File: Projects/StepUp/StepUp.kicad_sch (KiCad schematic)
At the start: 4 parts

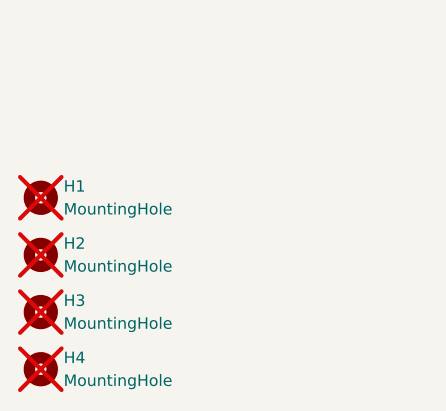
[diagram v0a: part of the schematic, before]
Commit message: feat(v0.2): Schematic updated, PCB layout start
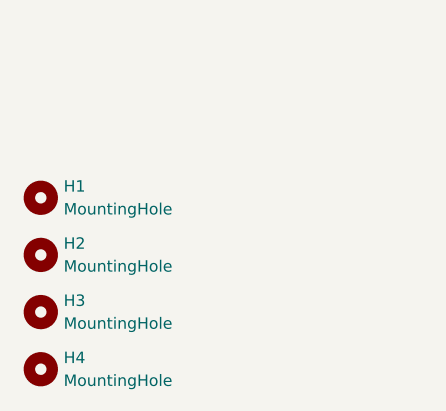
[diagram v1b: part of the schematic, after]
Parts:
- H1, H2, H3, H4: now fitted; now left out of the parts list
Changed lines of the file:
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@@
 		(title "System diagram")
 		(date "2024-04-28")
-		(rev "v0.1")
+		(rev "v0.2")
 		(company "SJFOM")
 	)
@@
 		(unit 1)
 		(exclude_from_sim no)
-		(in_bom yes)
-		(on_board yes)
-		(dnp yes)
+		(in_bom no)
+		(on_board yes)
+		(dnp no)
 		(fields_autoplaced yes)
 		(property "Reference" "H3"
@@
 		(unit 1)
 		(exclude_from_sim no)
-		(in_bom yes)
-		(on_board yes)
-		(dnp yes)
+		(in_bom no)
+		(on_board yes)
+		(dnp no)
 		(fields_autoplaced yes)
 		(property "Reference" "H4"
@@
 		(unit 1)
 		(exclude_from_sim no)
-		(in_bom yes)
-		(on_board yes)
-		(dnp yes)
+		(in_bom no)
+		(on_board yes)
+		(dnp no)
 		(fields_autoplaced yes)
 		(property "Reference" "H1"
@@
 		(unit 1)
 		(exclude_from_sim no)
-		(in_bom yes)
-		(on_board yes)
-		(dnp yes)
+		(in_bom no)
+		(on_board yes)
+		(dnp no)
 		(fields_autoplaced yes)
 		(property "Reference" "H2"

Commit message: feat(v0.2): Rough layout begins
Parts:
- H1, H2, H3, H4: footprint MountingHole:MountingHole_3.2mm_M3_DIN965_Pad -> MountingHole:MountingHole_2.2mm_M2

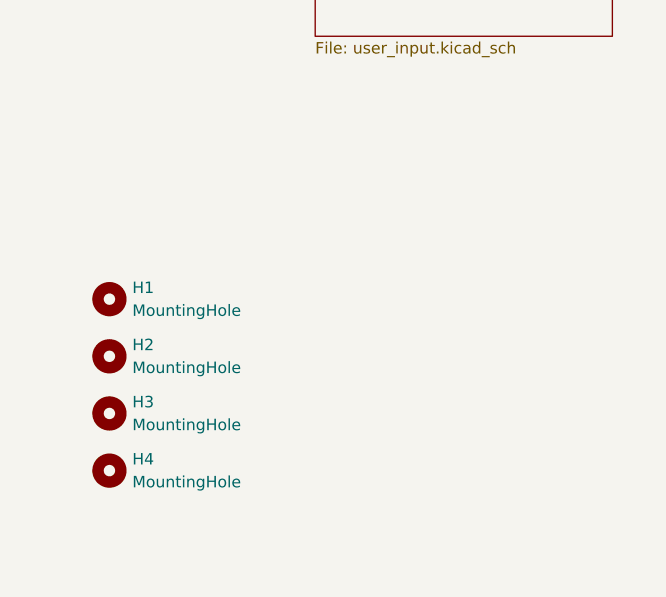
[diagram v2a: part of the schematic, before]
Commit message: feat(v0.2): Component layout from CAD
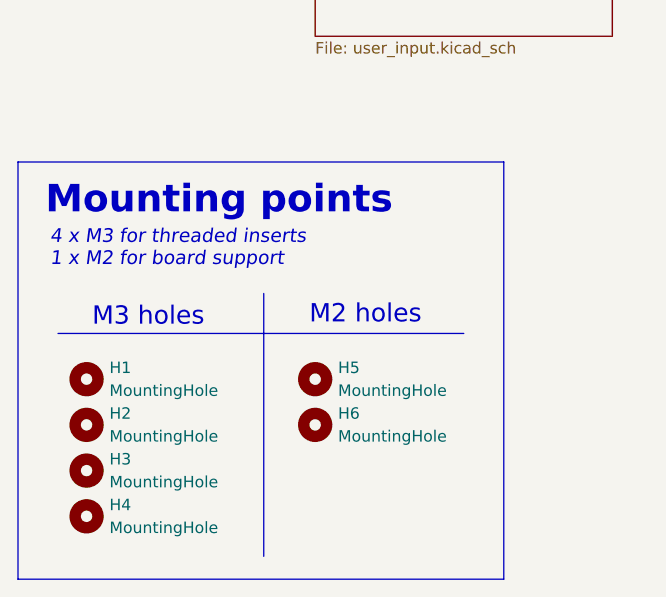
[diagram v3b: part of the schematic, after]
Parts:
- added H5, H6: MountingHole, MountingHole:MountingHole_2.2mm_M2, symbol Mechanical:MountingHole
- H1, H2, H3, H4: footprint MountingHole:MountingHole_2.2mm_M2 -> MountingHole:MountingHole_3.2mm_M3_DIN965
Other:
- note added: "4 x M3 for threaded inserts 1 x M2 for board support"
- note added: "M2 holes"
- note added: "M3 holes"
- note added: "Mounting points"

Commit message: feat(v0.2): Release, PCBs ordered!
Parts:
- added FID1, FID2, FID3: Fiducial, Fiducial:Fiducial_1mm_Mask2mm, symbol Mechanical:Fiducial
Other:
- note added: "Fiducials"

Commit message: feat(v0.3): Minor updates for PCBWay order
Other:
- note added: "M3 for threaded inserts M2 for board support"
- note removed: "4 x M3 for threaded inserts 1 x M2 for board support"
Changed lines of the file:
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@@
 		)
 	)
-	(text "4 x M3 for threaded inserts\n1 x M2 for board support"
+	(text "M3 for threaded inserts\nM2 for board support"
 		(exclude_from_sim no)
 		(at 26.416 154.432 0)
